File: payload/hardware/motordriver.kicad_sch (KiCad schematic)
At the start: 5 parts, among them U3 CD74HC4067SM

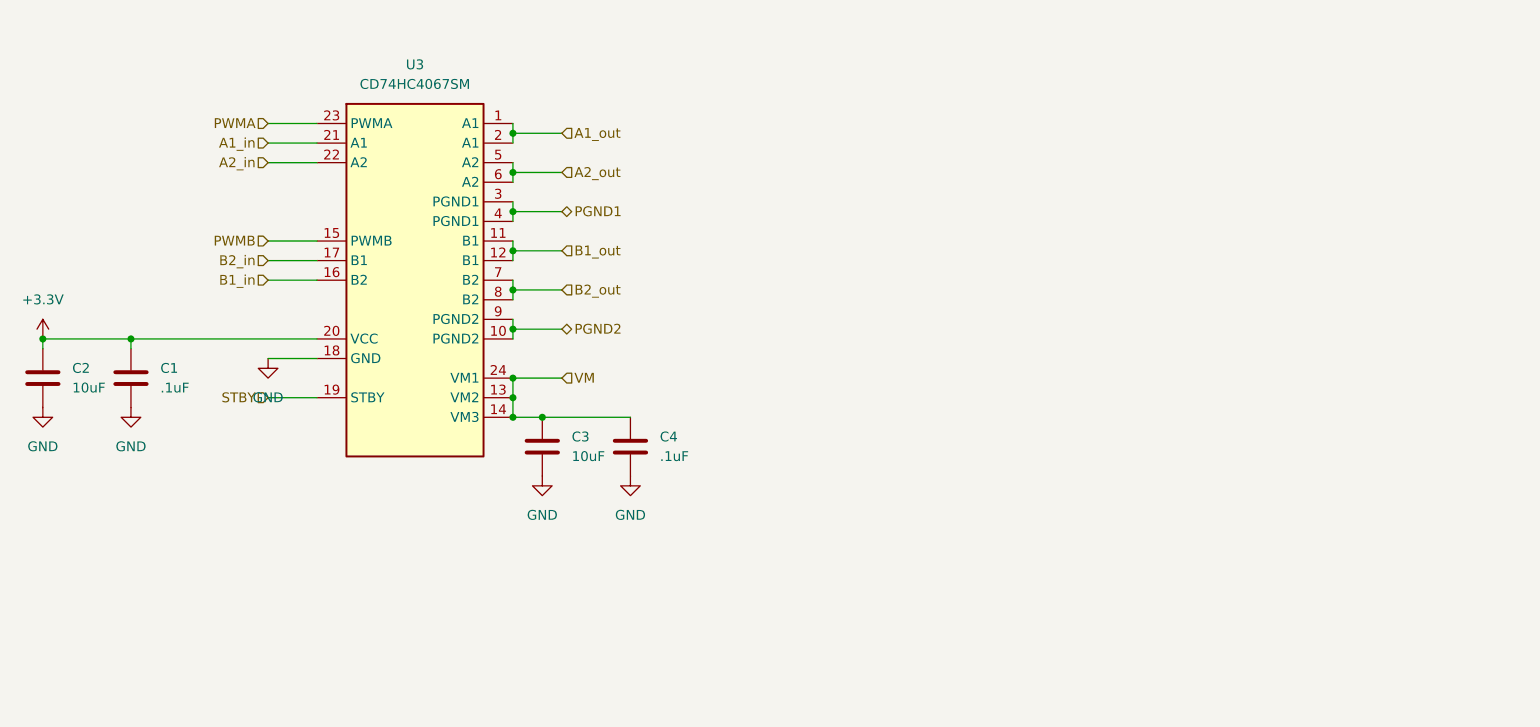
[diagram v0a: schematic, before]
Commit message: add part of a motor driver
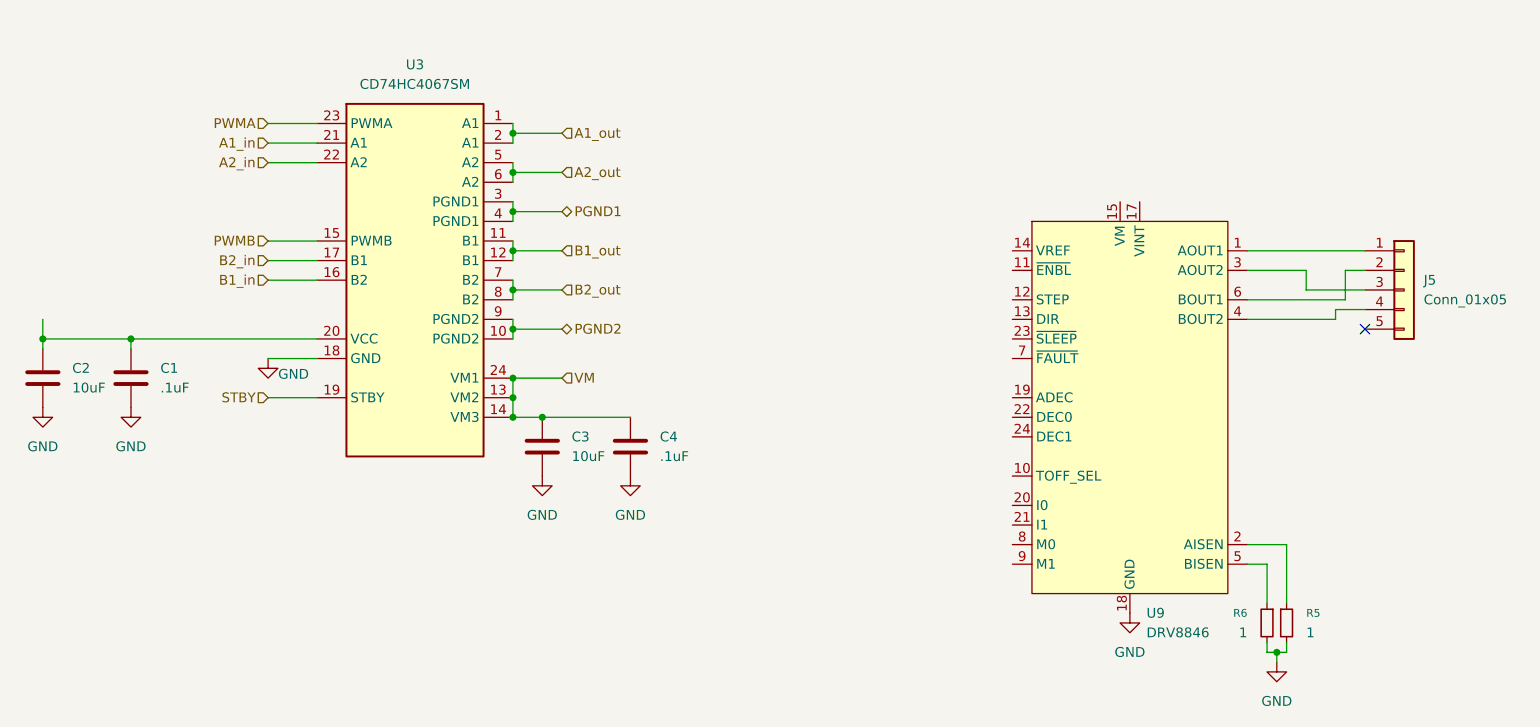
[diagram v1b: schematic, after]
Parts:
- added J5: Conn_01x05, Connector_JST:JST_XH_B5B-XH-AM_1x05_P2.50mm_Vertical, symbol Connector_Generic:Conn_01x05
- added R5, R6: 1, Resistor_SMD:R_1206_3216Metric, symbol Device:R_Small
- added U9: DRV8846, Package_DFN_QFN:VQFN-24-1EP_4x4mm_P0.5mm_EP2.45x2.45mm_ThermalVias, symbol payload-syms:DRV8846
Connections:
- net GND: now also R5.2, R6.2, U9.18 (GND), U9.25 (GND)
- net +3.3V: no longer names the net of C1.1, C2.1, U3.20 (VCC)
- new net: J5.1 (Pin_1), U9.1 (AOUT1)
- new net: J5.2 (Pin_2), U9.6 (BOUT1)
- new net: J5.3 (Pin_3), U9.3 (AOUT2)
- new net: J5.4 (Pin_4), U9.4 (BOUT2)
- new net: R5.1, U9.2 (AISEN)
- new net: R6.1, U9.5 (BISEN)
- no-connect marks 0 -> 1

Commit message: add ethernet
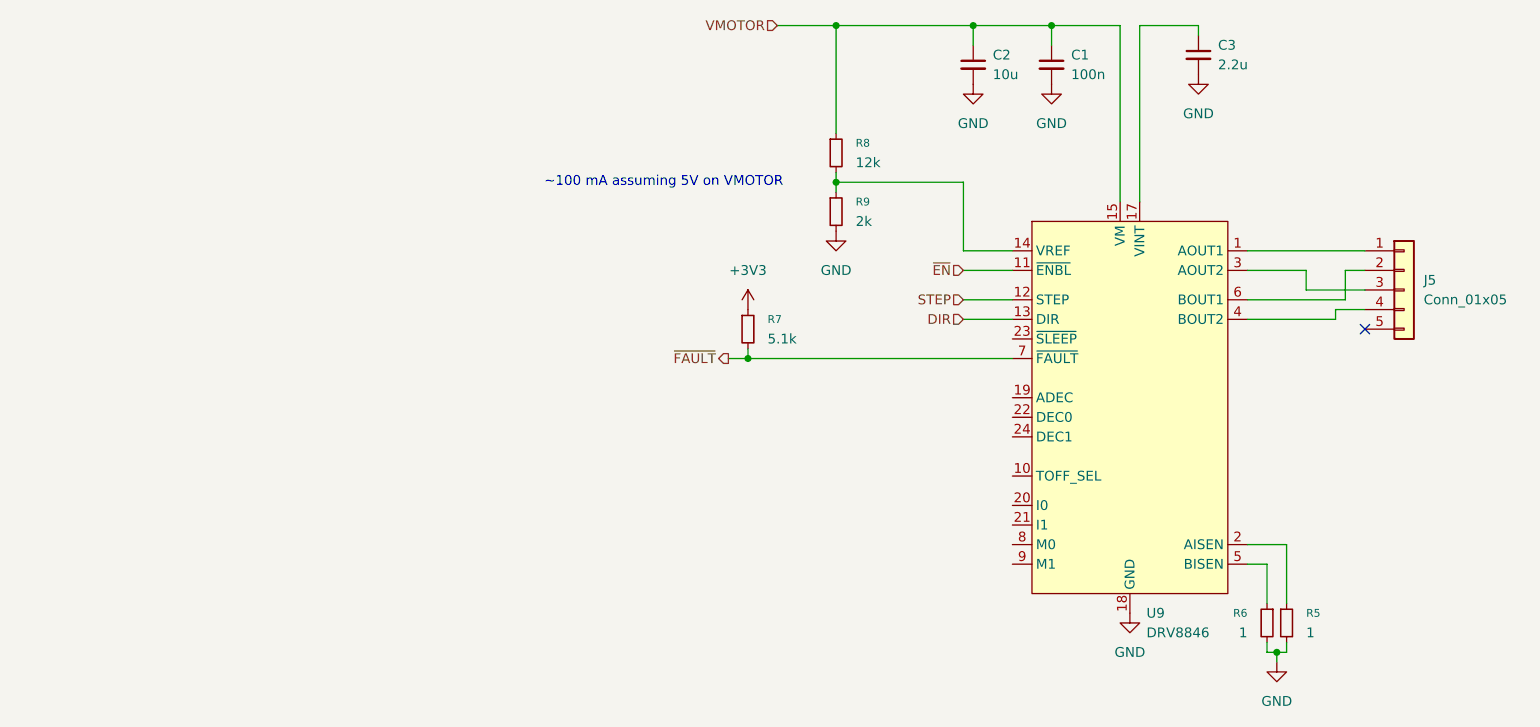
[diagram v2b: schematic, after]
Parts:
- removed C1, C4: .1uF, Capacitor_SMD:C_0402_1005Metric, symbol Device:C
- removed C2, C3: 10uF, Capacitor_SMD:C_0402_1005Metric, symbol Device:C
- removed U3: CD74HC4067SM, Package_SO:SSOP-24_5.3x8.2mm_P0.65mm, symbol 74xx:CD74HC4067SM
- added C1: 100n, Capacitor_SMD:C_0402_1005Metric, symbol Device:C_Small
- added C2: 10u, Capacitor_SMD:C_0402_1005Metric, symbol Device:C_Small
- added C3: 2.2u, Capacitor_SMD:C_0402_1005Metric, symbol Device:C_Small
- added R7: 5.1k, Resistor_SMD:R_0402_1005Metric, symbol Device:R_Small
- added R8: 12k, Resistor_SMD:R_0402_1005Metric, symbol Device:R_Small
- added R9: 2k, Resistor_SMD:R_0402_1005Metric, symbol Device:R_Small
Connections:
- net GND: now also C1.2, C2.2, C3.2, R9.2
- net ~{EN}: now reaches U9.11 (~{ENBL})
- net STEP: now reaches U9.12 (STEP)
- net DIR: now reaches U9.13 (DIR)
- net at U9.14 (VREF): now also R8.2, R9.1
- net VMOTOR: now reaches U9.15 (VM)
- net VMOTOR: now also C1.1, C2.1, R8.1
- net at U9.17 (VINT): now also C3.1
- net ~{FAULT}: now reaches U9.7 (~{FAULT})
- net ~{FAULT}: now also R7.2
- new net +3V3: R7.1
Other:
- note added: "~100 mA assuming 5V on VMOTOR"

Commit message: finish CANbus schematic and fix USB
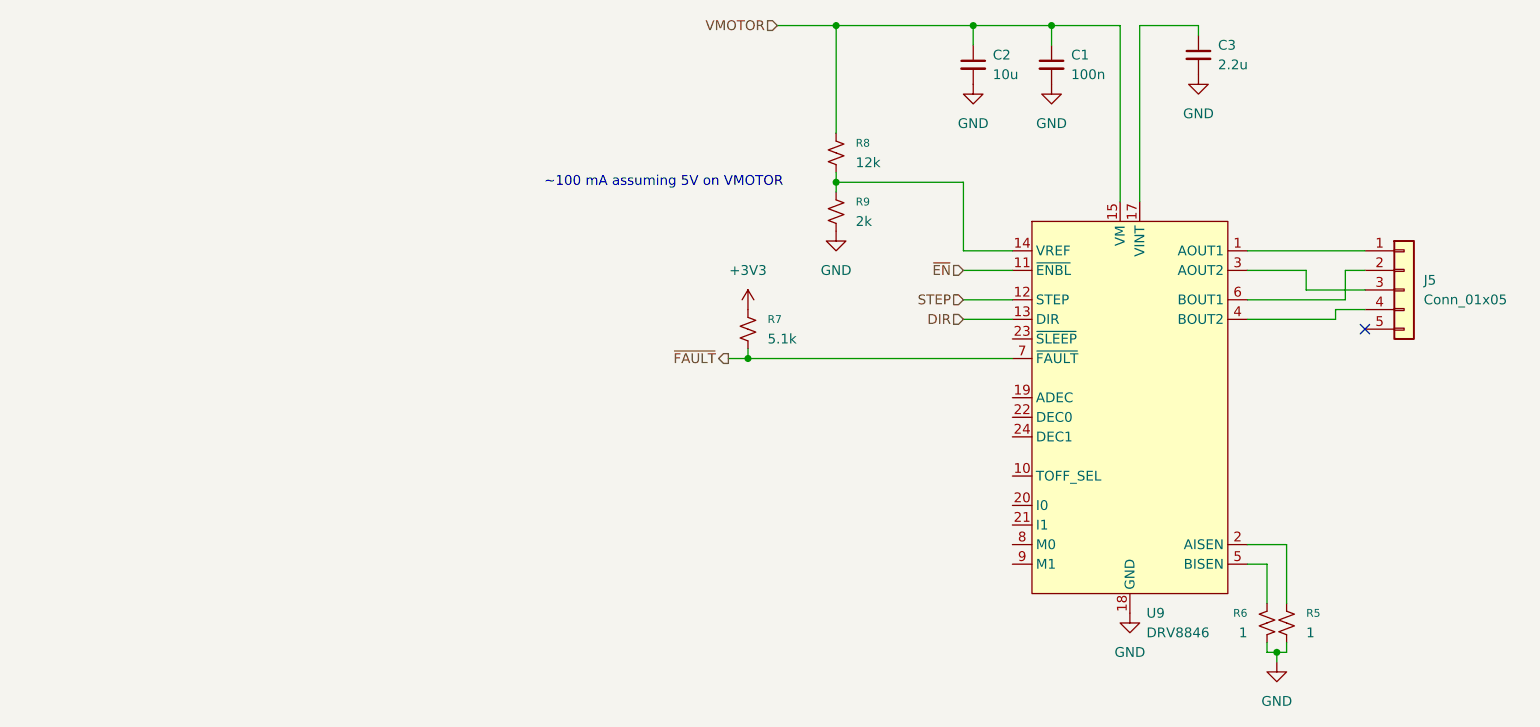
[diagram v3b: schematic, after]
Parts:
- R5, R6, R7, R8, R9: symbol Device:R_Small -> Device:R_Small_US
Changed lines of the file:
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@@
 	)
 	(symbol
-		(lib_id "Device:R_Small")
+		(lib_id "Device:R_Small_US")
 		(at 180.34 63.5 0)
 		(unit 1)
@@
 			)
 		)
-		(property "Description" "Resistor, small symbol"
+		(property "Description" "Resistor, small US symbol"
 			(at 180.34 63.5 0)
 			(hide yes)
@@
 	)
 	(symbol
-		(lib_id "Device:R_Small")
+		(lib_id "Device:R_Small_US")
 		(at 180.34 71.12 0)
 		(unit 1)
@@
 			)
 		)
-		(property "Description" "Resistor, small symbol"
+		(property "Description" "Resistor, small US symbol"
 			(at 180.34 71.12 0)
 			(hide yes)
@@
 	)
 	(symbol
-		(lib_id "Device:R_Small")
+		(lib_id "Device:R_Small_US")
 		(at 236.22 124.46 0)
 		(mirror y)
@@
 			)
 		)
-		(property "Description" "Resistor, small symbol"
+		(property "Description" "Resistor, small US symbol"
 			(at 236.22 124.46 0)
 			(hide yes)
@@
 	)
 	(symbol
-		(lib_id "Device:R_Small")
+		(lib_id "Device:R_Small_US")
 		(at 168.91 86.36 0)
 		(unit 1)
@@
 			)
 		)
-		(property "Description" "Resistor, small symbol"
+		(property "Description" "Resistor, small US symbol"
 			(at 168.91 86.36 0)
 			(hide yes)
@@
 	)
 	(symbol
-		(lib_id "Device:R_Small")
+		(lib_id "Device:R_Small_US")
 		(at 238.76 124.46 0)
 		(unit 1)
@@
 			)
 		)
-		(property "Description" "Resistor, small symbol"
+		(property "Description" "Resistor, small US symbol"
 			(at 238.76 124.46 0)
 			(hide yes)

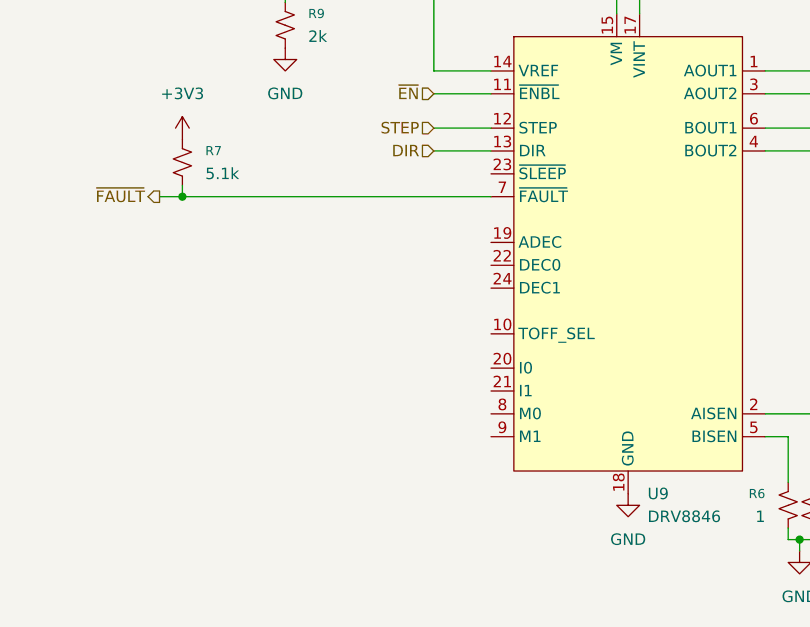
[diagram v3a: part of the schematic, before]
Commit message: motor driver schematic, work on high speed routing
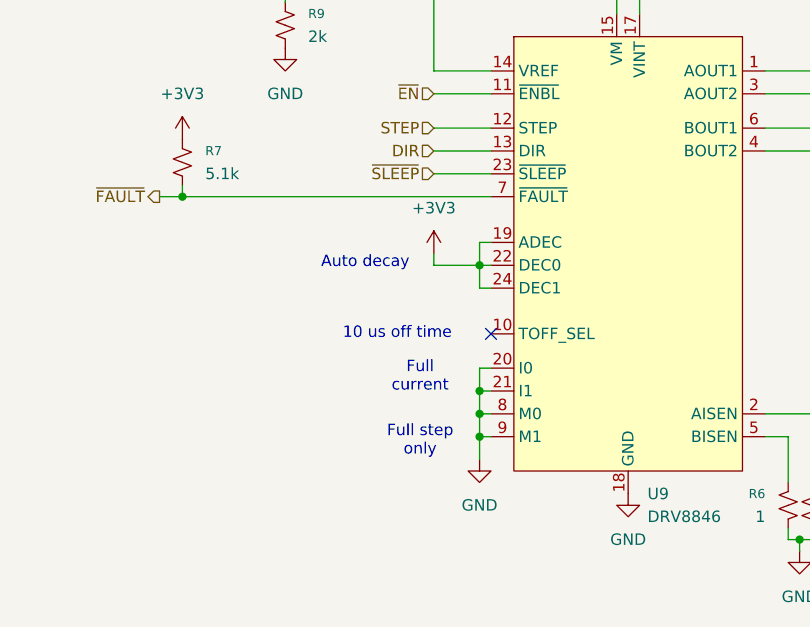
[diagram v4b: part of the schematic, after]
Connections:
- net +3V3: now also U9.19 (ADEC), U9.22 (DEC0), U9.24 (DEC1)
- net GND: now also U9.20 (I0), U9.21 (I1), U9.8 (M0), U9.9 (M1)
- net ~{SLEEP}: now reaches U9.23 (~{SLEEP})
- no-connect marks 1 -> 2
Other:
- note added: "10 us off time"
- note added: "Auto decay"
- note added: "Full current"
- note added: "Full step only"

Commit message: ERC fixes, nits, NC
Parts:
- C1, C2, C3: symbol Device:C_Small -> Device:C_Small_US
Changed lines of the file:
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@@
 	)
 	(symbol
-		(lib_id "Device:C_Small")
+		(lib_id "Device:C_Small_US")
 		(at 198.12 52.07 0)
 		(unit 1)
@@
 		(fields_autoplaced yes)
 		(property "Reference" "C2"
-			(at 200.66 50.8062 0)
+			(at 200.66 50.9269 0)
 			(show_name no)
 			(do_not_autoplace no)
@@
 		)
 		(property "Value" "10u"
-			(at 200.66 53.3462 0)
+			(at 200.66 53.4669 0)
 			(show_name no)
 			(do_not_autoplace no)
@@
 			)
 		)
-		(property "Description" "Unpolarized capacitor, small symbol"
+		(property "Description" "capacitor, small US symbol"
 			(at 198.12 52.07 0)
 			(hide yes)
@@
 	)
 	(symbol
-		(lib_id "Device:C_Small")
+		(lib_id "Device:C_Small_US")
 		(at 227.33 50.8 0)
 		(unit 1)
@@
 		(fields_autoplaced yes)
 		(property "Reference" "C3"
-			(at 229.87 49.5362 0)
+			(at 229.87 49.6569 0)
 			(show_name no)
 			(do_not_autoplace no)
@@
 		)
 		(property "Value" "2.2u"
-			(at 229.87 52.0762 0)
+			(at 229.87 52.1969 0)
 			(show_name no)
 			(do_not_autoplace no)
@@
 			)
 		)
-		(property "Description" "Unpolarized capacitor, small symbol"
+		(property "Description" "capacitor, small US symbol"
 			(at 227.33 50.8 0)
 			(hide yes)
@@
 	)
 	(symbol
-		(lib_id "Device:C_Small")
+		(lib_id "Device:C_Small_US")
 		(at 208.28 52.07 0)
 		(unit 1)
@@
 		(fields_autoplaced yes)
 		(property "Reference" "C1"
-			(at 210.82 50.8062 0)
+			(at 210.82 50.9269 0)
 			(show_name no)
 			(do_not_autoplace no)
@@
 		)
 		(property "Value" "100n"
-			(at 210.82 53.3462 0)
+			(at 210.82 53.4669 0)
 			(show_name no)
 			(do_not_autoplace no)
@@
 			)
 		)
-		(property "Description" "Unpolarized capacitor, small symbol"
+		(property "Description" "capacitor, small US symbol"
 			(at 208.28 52.07 0)
 			(hide yes)

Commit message: add digikey part numbers
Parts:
- C1: Digikey (none) -> 1276-1001-1-ND
- C2: Digikey (none) -> 1276-CL05A106MP6NUN8CT-ND
- C3: Digikey (none) -> 490-10012-1-ND
- J5: Digikey (none) -> 455-B5B-XH-AM-ND
- R5, R6: Digikey (none) -> 541-1.00UCT-ND
- R7: Digikey (none) -> YAG3503CT-ND
- R8: Digikey (none) -> 13-RC0402FR-1312KLCT-ND
- R9: Digikey (none) -> 311-2KLRCT-ND
- U9: Digikey (none) -> 296-40083-1-ND
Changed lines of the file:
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@@
+			)
+		)
+		(property "Digikey" "455-B5B-XH-AM-ND"
+			(at 254 81.28 0)
+			(hide yes)
+			(show_name no)
+			(do_not_autoplace no)
+			(effects
+				(font
+					(size 1.27 1.27)
+				)
 			)
 		)
@@
 			)
 		)
+		(property "Digikey" "1276-CL05A106MP6NUN8CT-ND"
+			(at 198.12 52.07 0)
+			(hide yes)
+			(show_name no)
+			(do_not_autoplace no)
+			(effects
+				(font
+					(size 1.27 1.27)
+				)
+			)
+		)
 		(pin "2"
 		)
@@
 			)
 		)
+		(property "Digikey" "490-10012-1-ND"
+			(at 227.33 50.8 0)
+			(hide yes)
+			(show_name no)
+			(do_not_autoplace no)
+			(effects
+				(font
+					(size 1.27 1.27)
+				)
+			)
+		)
 		(pin "2"
 		)
@@
 			)
 		)
+		(property "Digikey" "13-RC0402FR-1312KLCT-ND"
+			(at 180.34 63.5 0)
+			(hide yes)
+			(show_name no)
+			(do_not_autoplace no)
+			(effects
+				(font
+					(size 1.27 1.27)
+				)
+			)
+		)
 		(pin "1"
 		)
@@
 			)
 		)
+		(property "Digikey" "311-2KLRCT-ND"
+			(at 180.34 71.12 0)
+			(hide yes)
+			(show_name no)
+			(do_not_autoplace no)
+			(effects
+				(font
+					(size 1.27 1.27)
+				)
+			)
+		)
 		(pin "1"
 		)
@@
 			)
 		)
+		(property "Digikey" "296-40083-1-ND"
+			(at 218.44 96.52 0)
+			(hide yes)
+			(show_name no)
+			(do_not_autoplace no)
+			(effects
+				(font
+					(size 1.27 1.27)
+				)
+			)
+		)
 		(pin "22"
 		)
@@
 			)
 		)
+		(property "Digikey" "1276-1001-1-ND"
+			(at 208.28 52.07 0)
+			(hide yes)
+			(show_name no)
+			(do_not_autoplace no)
+			(effects
+				(font
+					(size 1.27 1.27)
+				)
+			)
+		)
 		(pin "2"
 		)
@@
 			)
 		)
+		(property "Digikey" "541-1.00UCT-ND"
+			(at 236.22 124.46 0)
+			(hide yes)
+			(show_name no)
+			(do_not_autoplace no)
+			(effects
+				(font
+					(size 1.27 1.27)
+				)
+			)
+		)
 		(pin "1"
 		)
@@
 			)
 		)
+		(property "Digikey" "YAG3503CT-ND"
+			(at 168.91 86.36 0)
+			(hide yes)
+			(show_name no)
+			(do_not_autoplace no)
+			(effects
+				(font
+					(size 1.27 1.27)
+				)
+			)
+		)
 		(pin "1"
 		)
@@
 			(at 238.76 124.46 0)
 			(hide yes)
+			(show_name no)
+			(do_not_autoplace no)
+			(effects
+				(font
+					(size 1.27 1.27)
+				)
+			)
+		)
+		(property "Digikey" "541-1.00UCT-ND"
+			(at 238.76 124.46 0)
+			(hide yes)
